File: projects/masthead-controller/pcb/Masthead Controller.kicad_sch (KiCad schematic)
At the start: 219 parts, among them Q1 2N7002, Q2 2N7002, Q3 BSS138P,215, Q4 BSS138P,215, SW1 SW_MEC_5G, SW2 SW_MEC_5G

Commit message: Several v1.3.0 changes;
* CERN license corrected on PCB
* VR1's MODE/SYNC to R3 changed from +3.3V to new /VR1_vcc
* ROMs moved to sensor I2C bus
* New Config switch added (used to command DAC address config on power up if
  closed on boot)

Signed-off-by: digimer <digital.mermaid@gmail.com>
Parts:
- added C63: 0.1uF, mr-stuff:Kyocera AVX 0805, symbol mr-parts:Kyocera 08051C104K4Z2A
- added R50: 10kR, mr-stuff:Stackpole RNCP0805, symbol mr-parts:Stackpole RNCP0805FTD10K0
- added R51: 475R, mr-stuff:Stackpole RNCP0805, symbol mr-parts:Stackpole RNCP0805FTD475R
- added SW3: SW_MEC_5G, mr-stuff:SW_TS03-66-50-BK-160-LCR-D-67, symbol Switch:SW_MEC_5G
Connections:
- net +3.3V: now also R50.1; no longer R3.1
- net DAC_SCL: no longer ROM1.6 (SCL), ROM2.6 (SCL)
- net DAC_SDA: no longer ROM1.5 (SDA), ROM2.5 (SDA)
- net GND: now also C63.2, SW3.1 (A), SW3.2 (A)
- net I2C_SCL: now also ROM1.6 (SCL), ROM2.6 (SCL)
- net I2C_SDA: now also ROM1.5 (SDA), ROM2.5 (SDA)
- net VR1_VCC: now reaches C11.2, VR1.8 (VCC)
- net VR1_VCC: now also R3.1
- net CONFIG_SW: now reaches MCU1.31 (IO38)
- net CONFIG_SW: now also R51.2
- new net: C63.1, R50.2, R51.1, SW3.3 (B), SW3.4 (B)
- no-connect marks 11 -> 10
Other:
- note added: "Board Config Mode"
- note added: "Config"
- note added: "Configuration tasks, like DAC address changes, occur only if SW3 is closed during power up."
- note added: "Populate R3 _or_ R4, not both! R3: Forces PWM mode; consistent 2.2MHz switching. Noisier, but consistently so. VHF squelch may be quieter. R4: Auto mode; switches to PFM (bursts, 50 kHz) under 10~15% load (60~90mA). Expected that this board will live in that boundary, possibly resulting in frequent PWM <-> PFM transitions. Bench testing required."
- note removed: "Populate R3 _or_ R4, not both! R3: Forces PWM mode; consistent 2.2MHz switching. Noisier, but consistently so. VHF squelch may be quieter. R4: Auto mode; switches to PFM (bursts, 50 KHz) under 10~15% load (60~90mA). Expected that this board will live in that boundary, possibly resulting in frequent PWM <-> FPWM transitions. Bench testing required."
- moved on the sheet: R12, R13, TP3, TVS2

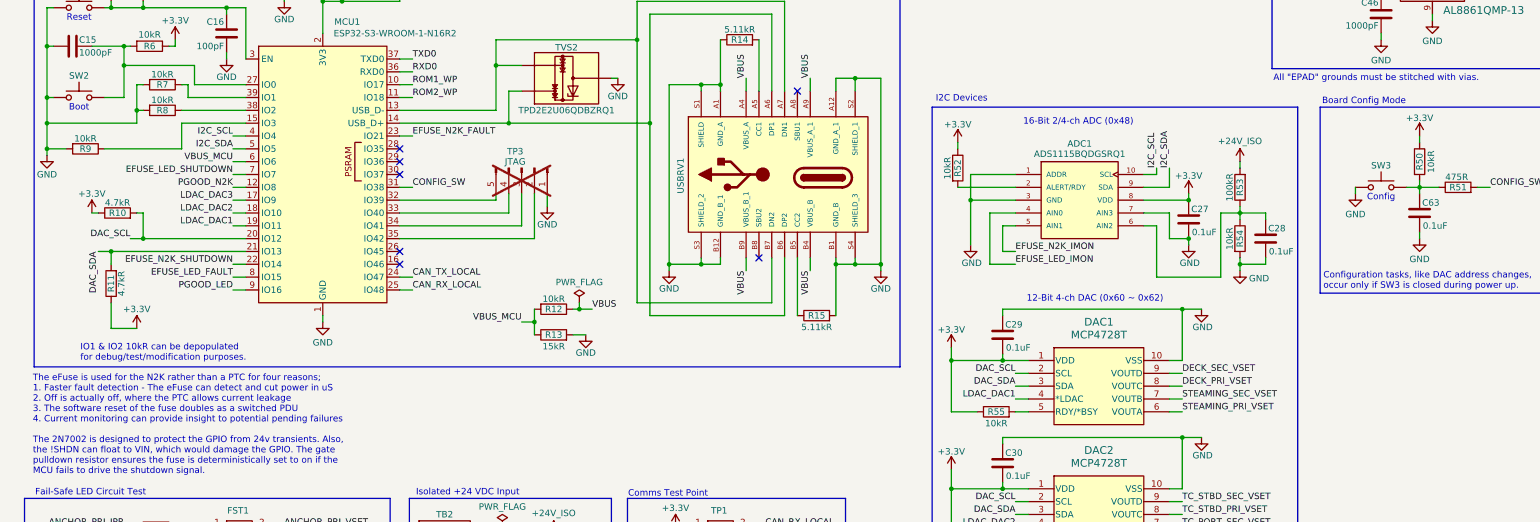
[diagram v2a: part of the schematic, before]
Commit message: Added pull-up resistors to I2C_S{DA,CL}.
Signed-off-by: digimer <digital.mermaid@gmail.com>
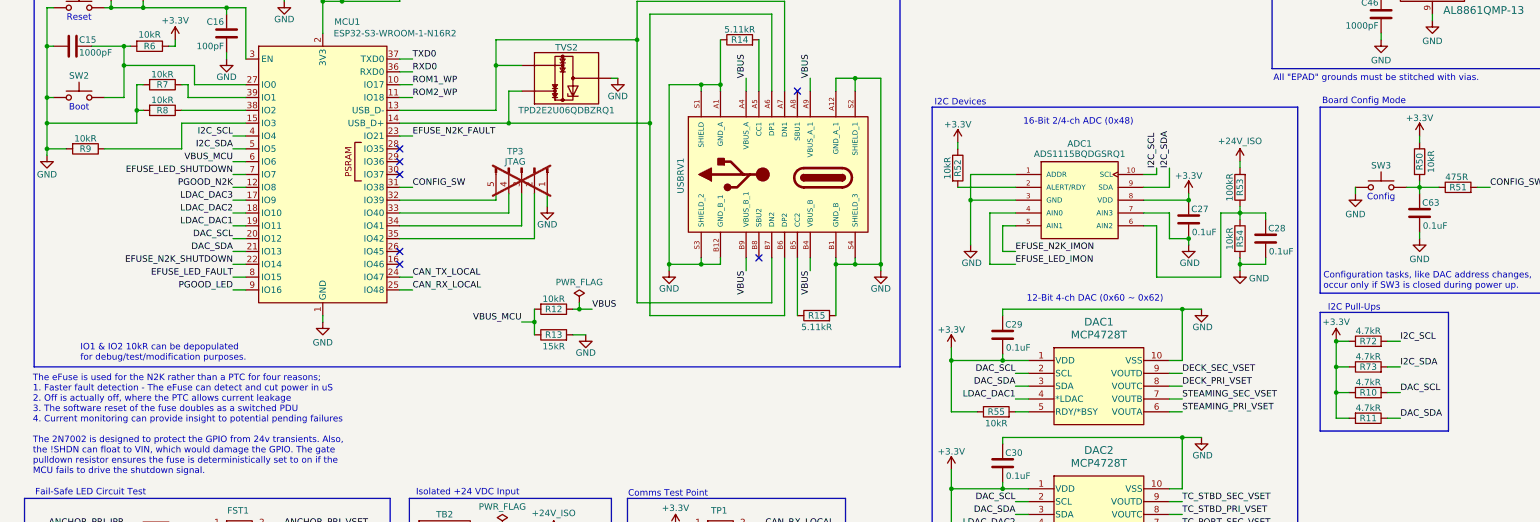
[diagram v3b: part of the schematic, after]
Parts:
- added R72, R73: 4.7kR, mr-stuff:Stackpole RMCA0805, symbol mr-parts:Stackpole RMCA0805FT4K70-HP
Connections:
- net +3.3V: now also R11.2, R72.1, R73.1; no longer R11.1
- net DAC_SDA: now also R11.1; no longer R11.2
- net I2C_SCL: now also R72.2
- net I2C_SDA: now also R73.2
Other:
- note added: "I2C Pull-Ups"

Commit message: Standadized LEDs and GPIO resistors.
* Settled on 475 Ohm current limiting resistors for GPIO.
* Settled on Vishay TLMS1101-GS15 SMD LEDs.
* Added an LED to the Masthead controller for various status applications.

Signed-off-by: digimer <digital.mermaid@gmail.com>
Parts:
- added LED1: TLMS1101-GS15, mr-stuff:Vishay TLMS1101, symbol mr-parts:Vishay TLMS1101-GS15
- added R75: 475R, mr-stuff:Stackpole RNCP0805, symbol mr-parts:Stackpole RNCP0805FTD475R
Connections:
- net GND: now also LED1.1 (K)
- net STATUS_LED: now reaches MCU1.30 (IO37)
- net STATUS_LED: now also R75.1
- new net: LED1.2 (A), R75.2
- no-connect marks 10 -> 9
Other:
- moved on the sheet: R10, R11, R72, R73

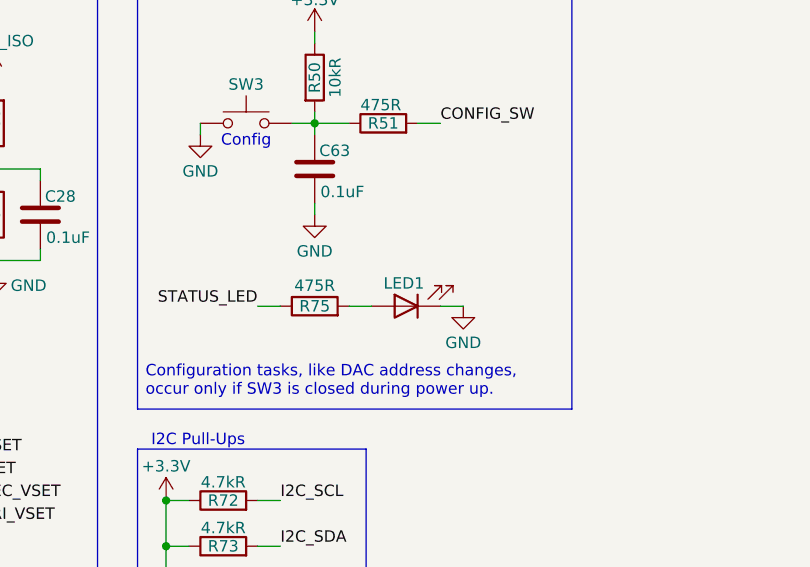
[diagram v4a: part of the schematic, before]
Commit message: Fixed Vishay TLMS1101-GS15 symbol.
Actually swapped the LEDs on the N2K transceiver.

Signed-off-by: digimer <digital.mermaid@gmail.com>
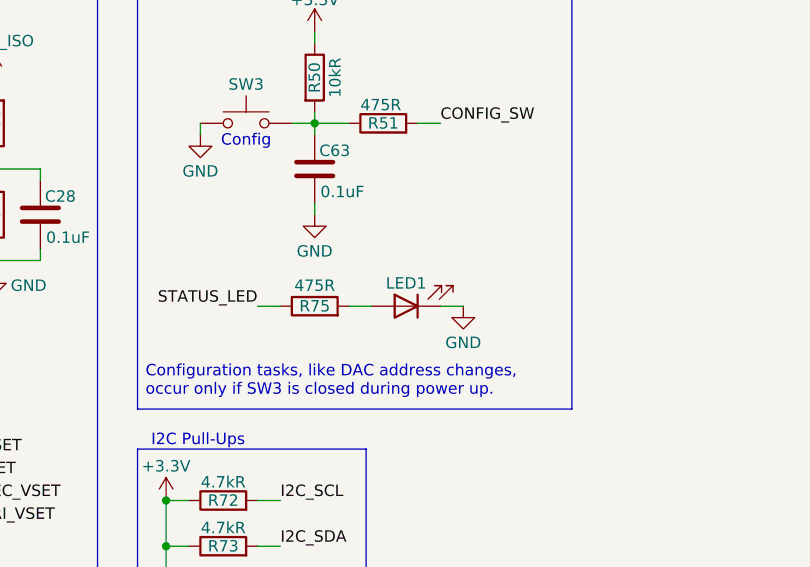
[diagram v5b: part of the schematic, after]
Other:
- moved on the sheet: LED1
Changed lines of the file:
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@@
 	(symbol
 		(lib_id "mr-parts:Vishay TLMS1101-GS15")
-		(at 299.72 219.71 180)
+		(at 299.72 219.71 0)
 		(unit 1)
 		(body_style 1)
@@
 		(dnp no)
 		(property "Reference" "LED1"
-			(at 299.466 217.17 0)
+			(at 299.72 217.17 0)
 			(show_name no)
 			(do_not_autoplace no)
@@
 		)
 		(property "Value" "TLMS1101-GS15"
-			(at 301.625 214.63 0)
+			(at 297.815 224.79 0)
 			(hide yes)
 			(show_name no)
@@
 		)
 		(property "Footprint" "mr-stuff:Vishay TLMS1101"
-			(at 299.72 206.502 0)
+			(at 299.72 232.918 0)
 			(hide yes)
 			(show_name no)
@@
 		)
 		(property "Datasheet" "https://www.vishay.com/docs/83173/tlmx1100.pdf"
-			(at 299.72 213.614 0)
+			(at 299.72 225.806 0)
 			(hide yes)
 			(show_name no)
@@
 		)
 		(property "Description" "Light emitting diode"
-			(at 299.72 208.788 0)
+			(at 299.72 230.632 0)
 			(hide yes)
 			(show_name no)
@@
 		)
 		(property "Part" "Vishay TLMS1101-GS15"
-			(at 299.72 211.074 0)
+			(at 299.72 228.346 0)
 			(hide yes)
 			(show_name no)

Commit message: Changed spreader lights to fail-off.
Signed-off-by: digimer <digital.mermaid@gmail.com>
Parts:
- added R74, R76: 4.7kR, mr-stuff:Stackpole RMCA0805, symbol mr-parts:Stackpole RMCA0805FT4K70-HP
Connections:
- net DECK_PRI_JPR: now also R76.1
- net DECK_SEC_JPR: now also R74.1
- net GND: now also R74.2, R76.2
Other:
- note added: "Pull-Up/Pull-Down Resistors"
- note added: "Spreader VSET lines pulled to GND to keep them off in a fail-safe condition. Deck lights could harm night time navigation."
- note removed: "I2C Pull-Ups"
- note removed: "Output is CC to prevent stobing on camera, LEDs are driven constantly without PWM."

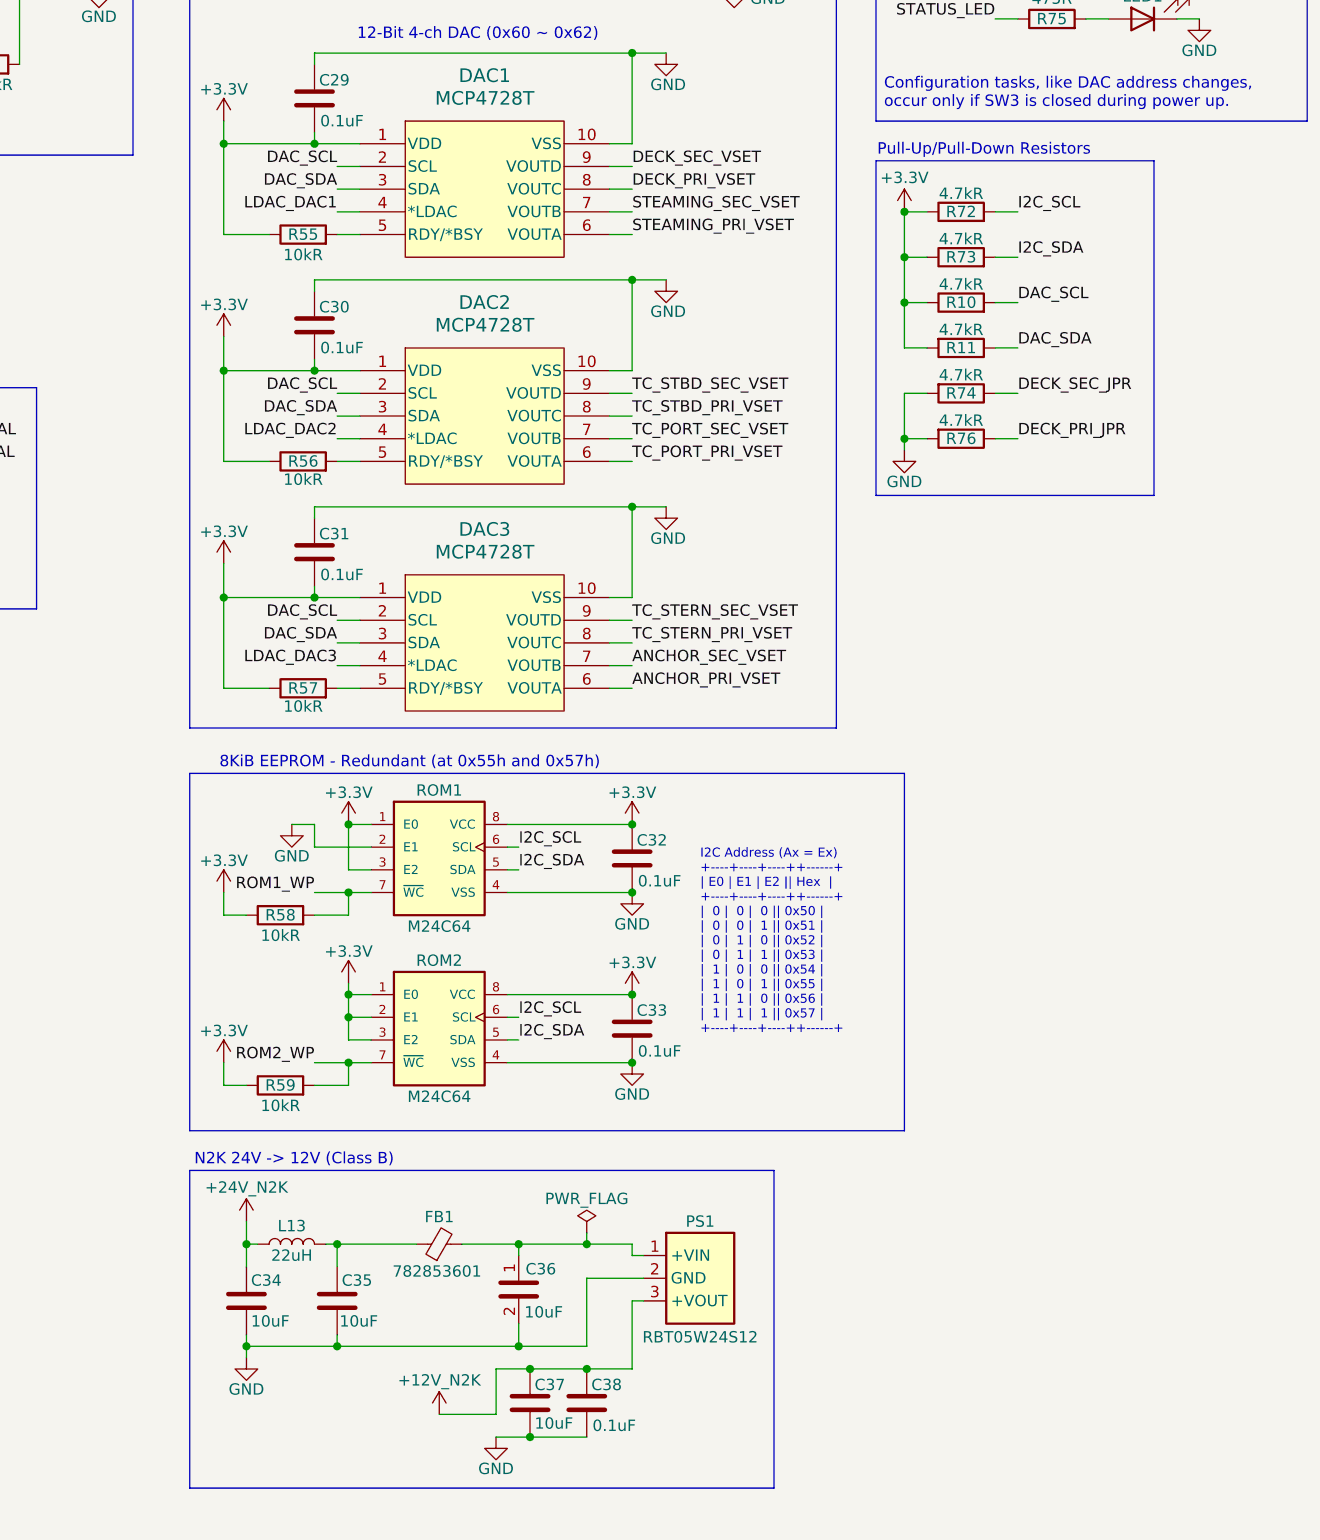
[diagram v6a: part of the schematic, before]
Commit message: Swapped the ROM on the MCTL to 128 KiB.
Swapped the I2C Pull-ups on the n2k-transceiver to 4.7kR.

Signed-off-by: digimer <digital.mermaid@gmail.com>
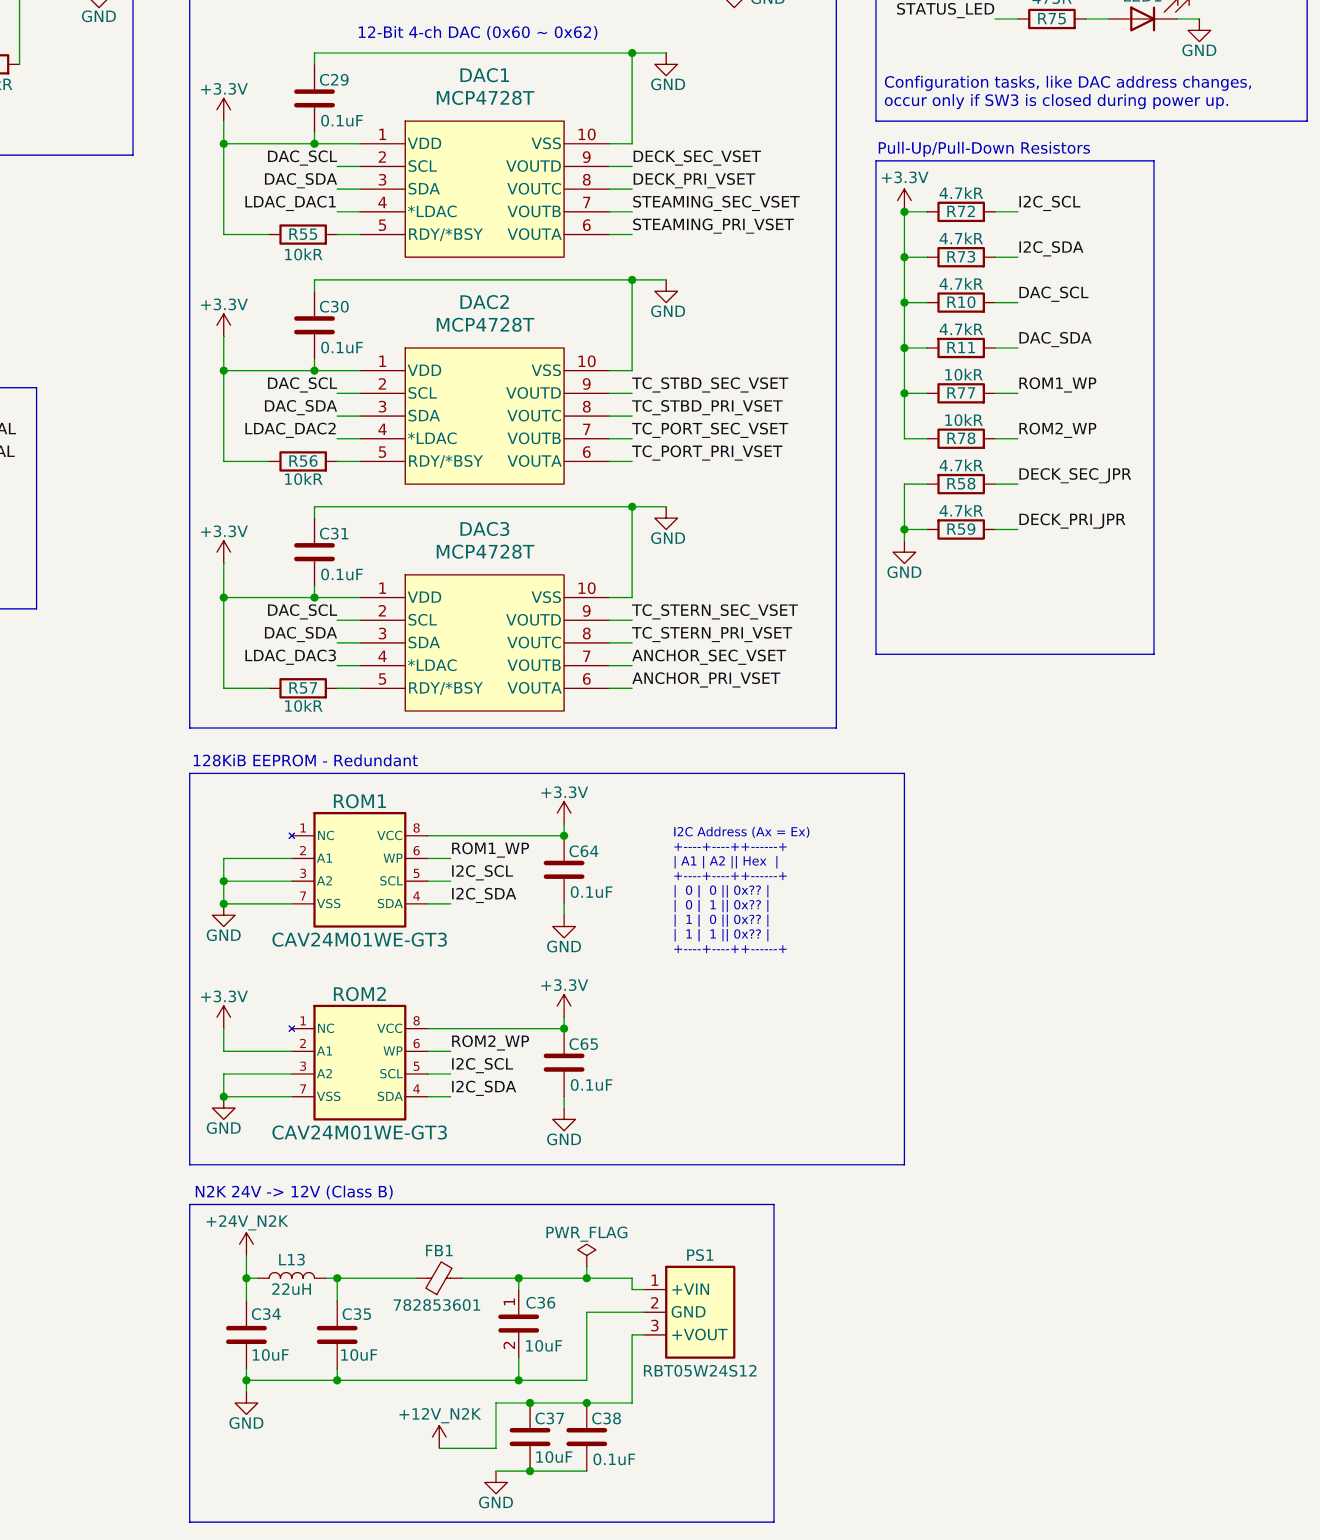
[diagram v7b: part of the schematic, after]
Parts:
- removed C32, C33: 0.1uF, mr-stuff:Kyocera AVX 0805, symbol mr-parts:Kyocera 08051C104K4Z2A
- removed R58, R59: 10kR, mr-stuff:Stackpole RNCP0805, symbol mr-parts:Stackpole RNCP0805FTD10K0
- removed ROM1, ROM2: M24C64, mr-stuff:STM M24C64-RMN6P, symbol mr-parts:STM_M24C64-RMN6P
- added C64, C65: 0.1uF, mr-stuff:Kyocera AVX 0805, symbol mr-parts:Kyocera 08051C104K4Z2A
- added R77, R78: 10kR, mr-stuff:Stackpole RNCP0805, symbol mr-parts:Stackpole RNCP0805FTD10K0
- added ROM1, ROM2: CAV24M01WE-GT3, symbol mr-parts:Onsemi CAV24M01WE-GT3
- renumbered R74 to R58, R76 to R59
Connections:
- net +3.3V: now also C64.1, C65.1, R77.1, R78.1, ROM1.8 (VCC), ROM2.2 (A1), ROM2.8 (VCC)
- net GND: now also C64.2, C65.2, ROM1.2 (A1), ROM1.3 (A2), ROM1.7 (VSS), ROM2.3 (A2), ROM2.7 (VSS)
- net I2C_SCL: now also ROM1.5 (SCL), ROM2.5 (SCL)
- net I2C_SDA: now also ROM1.4 (SDA), ROM2.4 (SDA)
- net ROM1_WP: now also R77.2, ROM1.6 (WP)
- net ROM2_WP: now also R78.2, ROM2.6 (WP)
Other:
- note added: "128KiB EEPROM - Redundant"
- note added: "I2C Address (Ax = Ex) +----+----++------+ | A1 | A2 || Hex | +----+----++------+ | 0 | 0 || 0x?? | | 0 | 1 || 0x?? | | 1 | 0 || 0x?? | | 1 | 1 || 0x?? | +----+----++------+"
- note removed: "8KiB EEPROM - Redundant (at 0x55h and 0x57h)"
- note removed: "I2C Address (Ax = Ex) +----+----+----++------+ | E0 | E1 | E2 || Hex | +----+----+----++------+ | 0 | 0 | 0 || 0x50 | | 0 | 0 | 1 || 0x51 | | 0 | 1 | 0 || 0x52 | | 0 | 1 | 1 || 0x53 | | 1 | 0 | 0 || 0x54 | | 1 | 0 | 1 || 0x55 | | 1 | 1 | 0 || 0x56 | | 1 | 1 | 1 || 0x57 | +----+----+----++------+"
- moved on the sheet: C34, C35, C36, C37, C38, FB1, L13, PS1, R58, R59
